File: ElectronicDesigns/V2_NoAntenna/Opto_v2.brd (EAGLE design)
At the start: 167 x 85.1 mm, 5 parts, among them U1 TLV1117-18IDCYG3

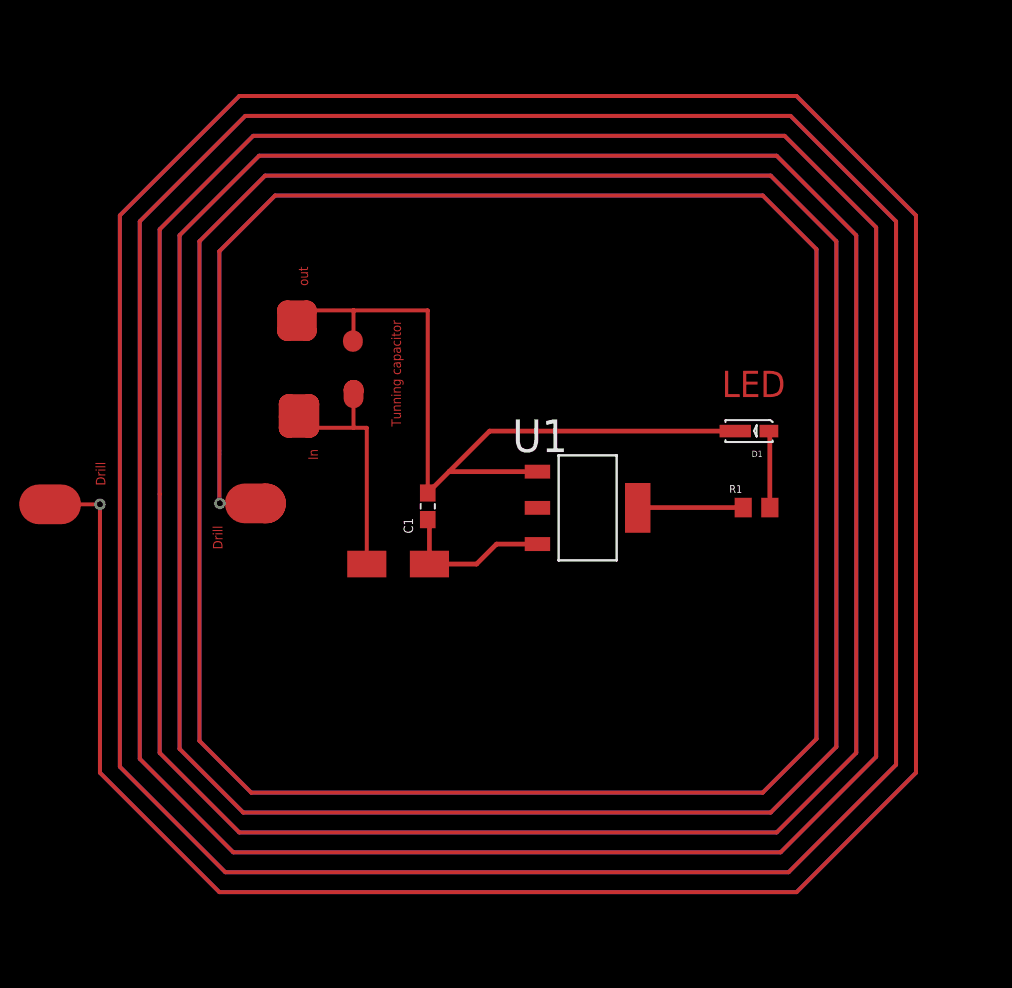
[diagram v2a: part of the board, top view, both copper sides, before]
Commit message: modify antenna
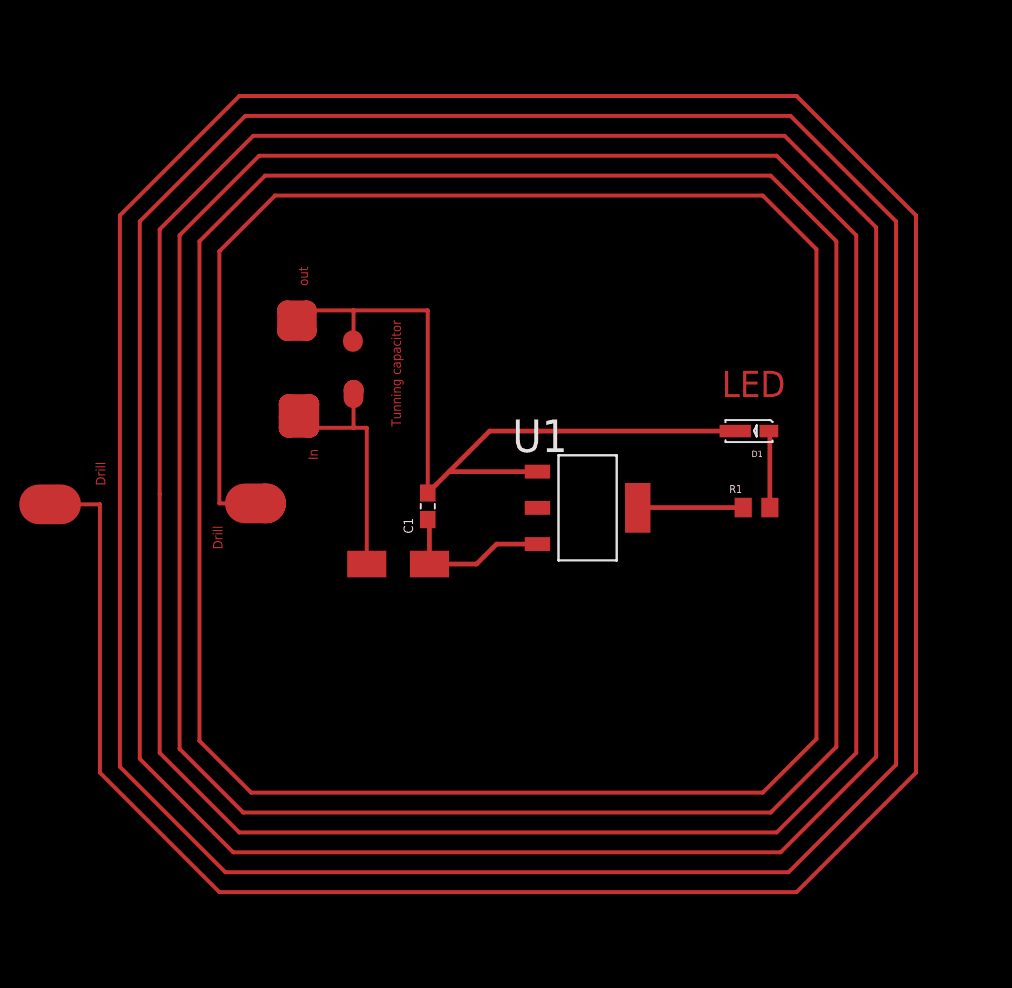
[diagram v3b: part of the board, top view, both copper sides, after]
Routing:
- net OUT: track 1073.1 -> 538.5 mm, vias 1 -> 0
- net IN: track 928.0 -> 465.6 mm, vias 1 -> 0
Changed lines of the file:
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@@
 <wire x1="42.329" y1="41.95" x2="39.85" y2="41.95" width="0.254" layer="1"/>
 <wire x1="39.85" y1="41.95" x2="38.445" y2="41.95" width="2.54" layer="1"/>
-<via x="42.329" y="41.95" extent="1-16" drill="0.35"/>
-<wire x1="42.329" y1="40.065" x2="42.329" y2="39.915" width="0.254" layer="16"/>
-<wire x1="42.329" y1="39.915" x2="42.329" y2="24.825" width="0.254" layer="16"/>
-<wire x1="49.949" y1="17.205" x2="42.329" y2="24.825" width="0.254" layer="16"/>
-<wire x1="49.949" y1="17.205" x2="86.779" y2="17.205" width="0.254" layer="16"/>
-<wire x1="86.779" y1="17.205" x2="94.399" y2="24.825" width="0.254" layer="16"/>
-<wire x1="94.399" y1="24.825" x2="94.399" y2="60.385" width="0.254" layer="16"/>
-<wire x1="94.399" y1="60.385" x2="86.779" y2="68.005" width="0.254" layer="16"/>
-<wire x1="86.779" y1="68.005" x2="51.219" y2="68.005" width="0.254" layer="16"/>
-<wire x1="51.219" y1="68.005" x2="43.599" y2="60.385" width="0.254" layer="16"/>
-<wire x1="43.599" y1="60.385" x2="43.599" y2="25.206" width="0.254" layer="16"/>
-<wire x1="43.599" y1="25.206" x2="50.33" y2="18.475" width="0.254" layer="16"/>
-<wire x1="50.33" y1="18.475" x2="86.271" y2="18.475" width="0.254" layer="16"/>
-<wire x1="86.271" y1="18.475" x2="93.129" y2="25.333" width="0.254" layer="16"/>
-<wire x1="93.129" y1="25.333" x2="93.129" y2="60.004" width="0.254" layer="16"/>
-<wire x1="93.129" y1="60.004" x2="86.398" y2="66.735" width="0.254" layer="16"/>
-<wire x1="86.398" y1="66.735" x2="51.6" y2="66.735" width="0.254" layer="16"/>
-<wire x1="51.6" y1="66.735" x2="44.869" y2="60.004" width="0.254" layer="16"/>
-<wire x1="44.869" y1="60.004" x2="44.869" y2="25.714" width="0.254" layer="16"/>
-<wire x1="44.869" y1="25.714" x2="50.838" y2="19.745" width="0.254" layer="16"/>
-<wire x1="50.838" y1="19.745" x2="85.763" y2="19.745" width="0.254" layer="16"/>
-<wire x1="85.763" y1="19.745" x2="91.859" y2="25.841" width="0.254" layer="16"/>
-<wire x1="91.859" y1="25.841" x2="91.859" y2="59.623" width="0.254" layer="16"/>
-<wire x1="91.859" y1="59.623" x2="86.017" y2="65.465" width="0.254" layer="16"/>
-<wire x1="86.017" y1="65.465" x2="52.108" y2="65.465" width="0.254" layer="16"/>
-<wire x1="52.108" y1="65.465" x2="46.139" y2="59.496" width="0.254" layer="16"/>
-<wire x1="46.139" y1="59.496" x2="46.139" y2="42.605" width="0.254" layer="16"/>
-<wire x1="42.329" y1="40.065" x2="42.329" y2="41.95" width="0.254" layer="16"/>
 </signal>
 <signal name="IN">
@@
 <wire x1="51.575" y1="42.01" x2="52.925" y2="42.01" width="2.54" layer="1"/>
 <wire x1="52.925" y1="42.01" x2="52.925" y2="42.005" width="2.54" layer="1"/>
-<wire x1="51.575" y1="42.01" x2="49.974" y2="42.01" width="0.254" layer="1"/>
-<via x="49.974" y="42.01" extent="1-16" drill="0.35"/>
+<wire x1="51.575" y1="42.01" x2="49.949" y2="42.01" width="0.254" layer="1"/>
 <wire x1="49.949" y1="58.099" x2="49.949" y2="42.01" width="0.254" layer="1"/>
-<wire x1="49.949" y1="42.01" x2="49.974" y2="42.01" width="0.254" layer="1"/>
-<wire x1="46.139" y1="26.095" x2="46.139" y2="42.605" width="0.254" layer="16"/>
-<wire x1="51.219" y1="21.015" x2="46.139" y2="26.095" width="0.254" layer="16"/>
-<wire x1="85.509" y1="21.015" x2="51.219" y2="21.015" width="0.254" layer="16"/>
-<wire x1="90.589" y1="26.095" x2="85.509" y2="21.015" width="0.254" layer="16"/>
-<wire x1="90.589" y1="59.115" x2="90.589" y2="26.095" width="0.254" layer="16"/>
-<wire x1="85.509" y1="64.195" x2="90.589" y2="59.115" width="0.254" layer="16"/>
-<wire x1="52.489" y1="64.195" x2="85.509" y2="64.195" width="0.254" layer="16"/>
-<wire x1="47.409" y1="59.115" x2="52.489" y2="64.195" width="0.254" layer="16"/>
-<wire x1="47.409" y1="26.349" x2="47.409" y2="59.115" width="0.254" layer="16"/>
-<wire x1="51.473" y1="22.285" x2="47.409" y2="26.349" width="0.254" layer="16"/>
-<wire x1="51.473" y1="22.285" x2="85.128" y2="22.285" width="0.254" layer="16"/>
-<wire x1="85.128" y1="22.285" x2="89.319" y2="26.476" width="0.254" layer="16"/>
-<wire x1="89.319" y1="26.476" x2="89.319" y2="58.734" width="0.254" layer="16"/>
-<wire x1="89.319" y1="58.734" x2="85.128" y2="62.925" width="0.254" layer="16"/>
-<wire x1="85.128" y1="62.925" x2="52.87" y2="62.925" width="0.254" layer="16"/>
-<wire x1="52.87" y1="62.925" x2="48.679" y2="58.734" width="0.254" layer="16"/>
-<wire x1="48.679" y1="58.734" x2="48.679" y2="26.857" width="0.254" layer="16"/>
-<wire x1="48.679" y1="26.857" x2="51.981" y2="23.555" width="0.254" layer="16"/>
-<wire x1="51.981" y1="23.555" x2="84.62" y2="23.555" width="0.254" layer="16"/>
-<wire x1="84.62" y1="23.555" x2="88.049" y2="26.984" width="0.254" layer="16"/>
-<wire x1="88.049" y1="26.984" x2="88.049" y2="58.226" width="0.254" layer="16"/>
-<wire x1="88.049" y1="58.226" x2="84.62" y2="61.655" width="0.254" layer="16"/>
-<wire x1="84.62" y1="61.655" x2="53.505" y2="61.655" width="0.254" layer="16"/>
-<wire x1="53.505" y1="61.655" x2="49.949" y2="58.099" width="0.254" layer="16"/>
-<wire x1="49.949" y1="58.099" x2="49.949" y2="45.365" width="0.254" layer="16"/>
-<wire x1="49.949" y1="45.365" x2="49.949" y2="45.145" width="0.254" layer="16"/>
-<wire x1="49.949" y1="45.145" x2="49.949" y2="42.035" width="0.254" layer="16"/>
-<wire x1="49.949" y1="42.035" x2="49.974" y2="42.01" width="0.254" layer="16"/>
 </signal>
 </signals>
